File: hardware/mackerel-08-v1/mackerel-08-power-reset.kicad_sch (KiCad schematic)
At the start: 43 parts, among them J10 Conn_02x03_Odd_Even, J5 Barrel_Jack_MountingPin, J6 Conn_02x03_Odd_Even, J7 Conn_02x03_Odd_Even, SW1 SW_Push, U15 LM2576T-5, U16 NE555P, U17 AP1084

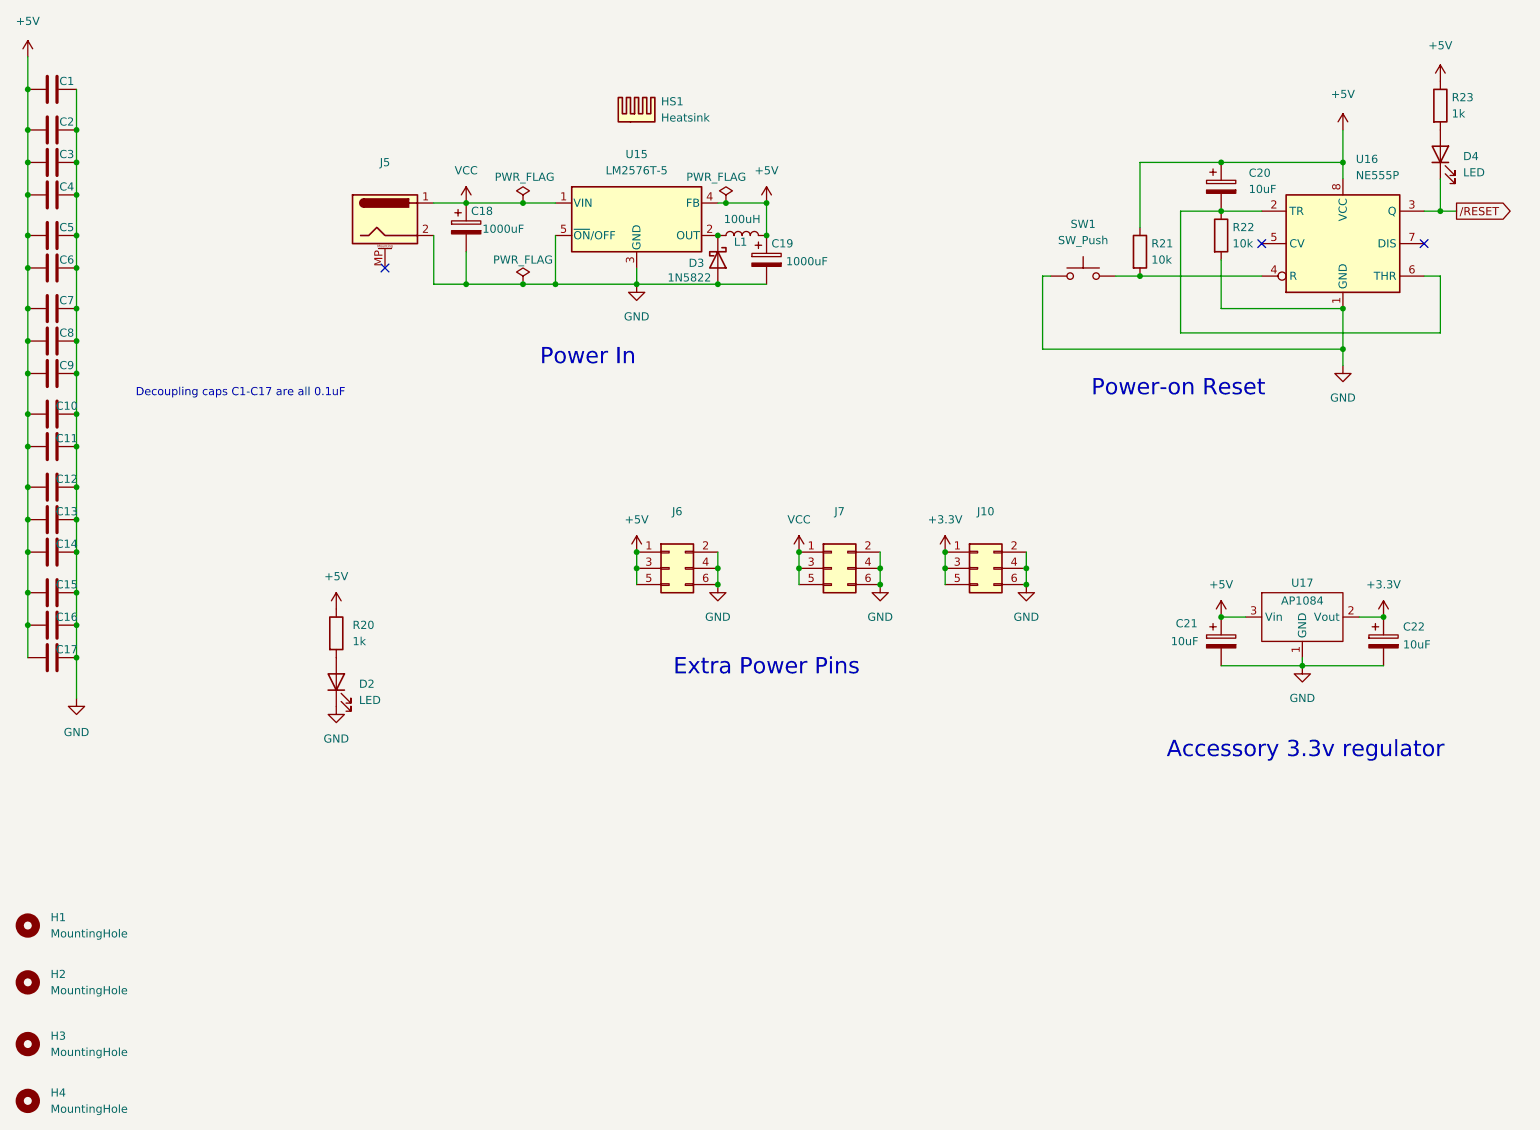
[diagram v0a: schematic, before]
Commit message: Mackerel-8: Remove 555 reset, 3.3v regulator, user LED
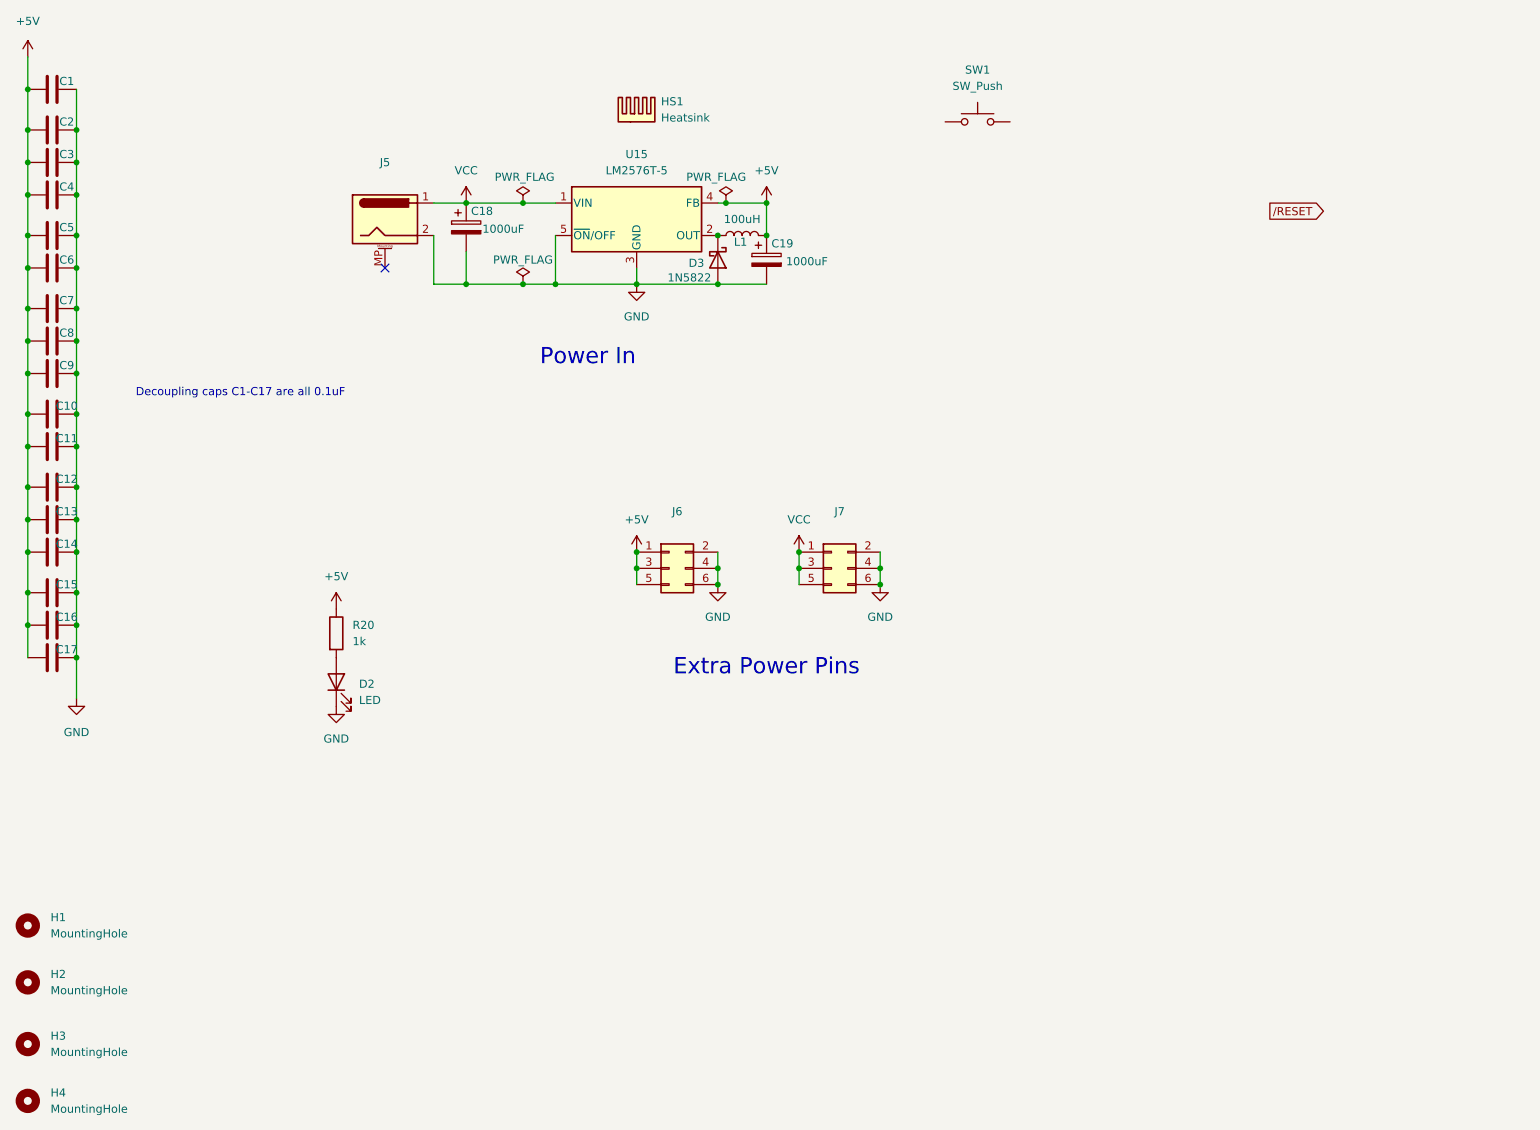
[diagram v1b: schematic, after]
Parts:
- removed C20, C21, C22: 10uF, Capacitor_THT:CP_Radial_D5.0mm_P2.50mm, symbol Device:C_Polarized
- removed D4: LED, LED_THT:LED_D5.0mm, symbol Device:LED
- removed J10: Conn_02x03_Odd_Even, Connector_PinHeader_2.54mm:PinHeader_2x03_P2.54mm_Vertical, symbol Connector_Generic:Conn_02x03_Odd_Even
- removed R21, R22: 10k, Resistor_SMD:R_1206_3216Metric_Pad1.30x1.75mm_HandSolder, symbol Device:R
- removed R23: 1k, Resistor_SMD:R_1206_3216Metric_Pad1.30x1.75mm_HandSolder, symbol Device:R
- removed U16: NE555P, Package_DIP:DIP-8_W7.62mm, symbol Timer:NE555P
- removed U17: AP1084, Package_TO_SOT_SMD:TO-252-2, symbol AP1084:AP1084
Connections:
- net GND: no longer SW1.1
- no-connect marks 3 -> 1
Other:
- note removed: "Accessory 3.3v regulator"
- note removed: "Power-on Reset"
- moved on the sheet: SW1
